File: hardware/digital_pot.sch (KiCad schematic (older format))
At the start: 100 parts, among them J8 Conn_02x08_Odd_Even, U10 MCP42010, U11 ADA4898-3, U12 ADA4898-3, U13 MCP42010, U14 MCP42010, U15 MCP42050, U16 MCP42050, U17 MCP42050, U2 ADA4898-3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

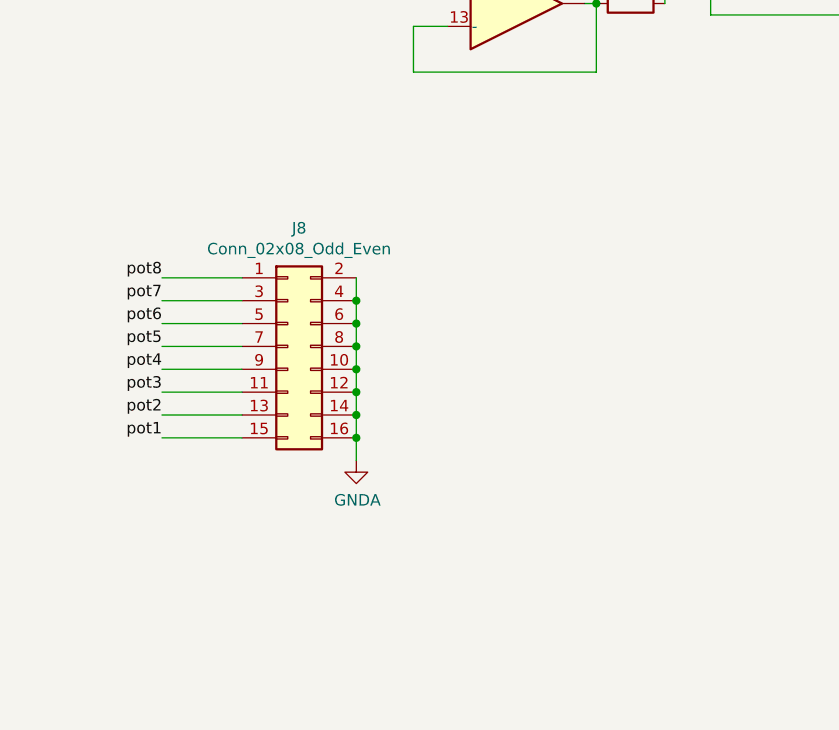
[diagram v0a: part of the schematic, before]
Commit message: layout gotów, do wyeliminowania błedy DRC
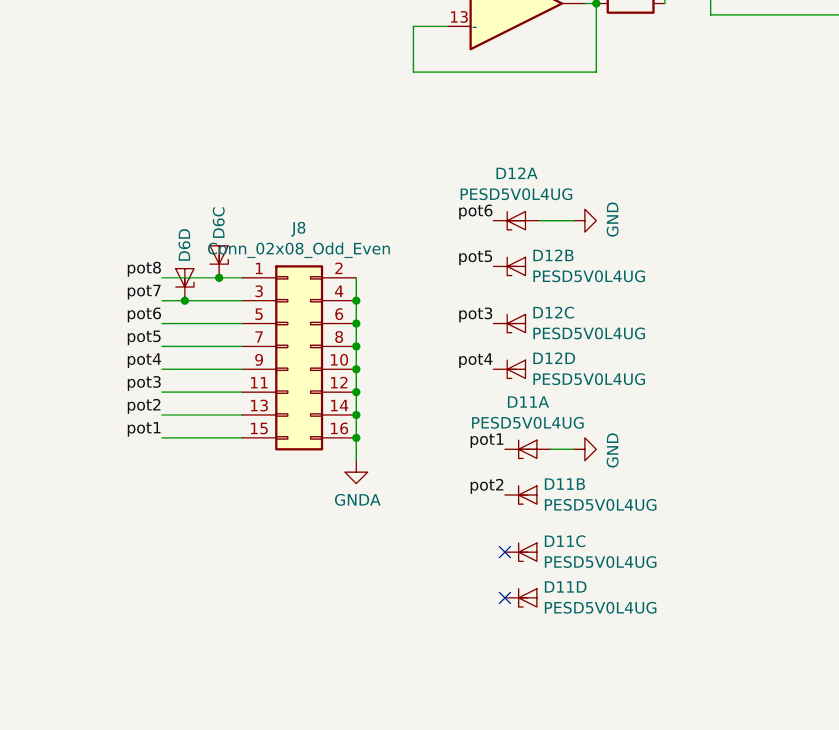
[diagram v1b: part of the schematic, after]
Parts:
- added D11, D12, D6: PESD5V0L4UG, Package_TO_SOT_SMD:SOT-353_SC-70-5, symbol Power_Protection:PESD5V0L4UG
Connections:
- net GND: now also D11.2 (A), D12.2 (A)
- net pot1: now also D11.1 (K1)
- net pot2: now also D11.3 (K2)
- net pot3: now also D12.4 (K3)
- net pot4: now also D12.5 (K4)
- net pot5: now also D12.3 (K2)
- net pot6: now also D12.1 (K1)
- net pot7: now also D6.5 (K4)
- net pot8: now also D6.4 (K3)
- no-connect marks 1 -> 3
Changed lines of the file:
@@
 	9500 9300 9850 9300
 Wire Wire Line
-	9850 9200 9500 9200
-Wire Wire Line
-	9500 9100 9850 9100
+	9850 9200 9600 9200
+Wire Wire Line
+	9500 9100 9750 9100
 Text Label 9500 9100 2    50   ~ 0
 pot8
@@
 Wire Wire Line
 	10350 9700 10350 9800
+$Comp
+L Power_Protection:PESD5V0L4UG D?
+U 3 1 5DD9CDD5
+P 9750 9000
+AR Path="/5CDEAB6D/5DD9CDD5" Ref="D?"  Part="3"
+AR Path="/5CDEABB2/5DD9CDD5" Ref="D6"  Part="3"
+F 0 "D6" H 9818 9000 50  0000 L CNN
+F 1 "PESD5V0L4UG" H 9818 8955 50  0001 L CNN
+F 2 "Package_TO_SOT_SMD:SOT-353_SC-70-5" H 9750 9000 50  0001 C CNN
+F 3 "https://assets.nexperia.com/documents/data-sheet/PESDXL4UF_G_W.pdf" H 9750 9000 50  0001 C CNN
+	3    9750 9000
+	0    -1   -1   0
+$EndComp
+$Comp
+L Power_Protection:PESD5V0L4UG D?
+U 4 1 5DD9CDDB
+P 9600 9100
+AR Path="/5CDEAB6D/5DD9CDDB" Ref="D?"  Part="4"
+AR Path="/5CDEABB2/5DD9CDDB" Ref="D6"  Part="4"
+F 0 "D6" H 9668 9100 50  0000 L CNN
+F 1 "PESD5V0L4UG" H 9668 9055 50  0001 L CNN
+F 2 "Package_TO_SOT_SMD:SOT-353_SC-70-5" H 9600 9100 50  0001 C CNN
+F 3 "https://assets.nexperia.com/documents/data-sheet/PESDXL4UF_G_W.pdf" H 9600 9100 50  0001 C CNN
+	4    9600 9100
+	0    -1   -1   0
+$EndComp
+Connection ~ 9750 9100
+Wire Wire Line
+	9750 9100 9850 9100
+Connection ~ 9600 9200
+Wire Wire Line
+	9600 9200 9500 9200
+$Comp
+L Power_Protection:PESD5V0L4UG D12
+U 1 1 5DE7618B
+P 11050 8850
+F 0 "D12" H 11050 9055 50  0000 C CNN
+F 1 "PESD5V0L4UG" H 11050 8964 50  0000 C CNN
+F 2 "Package_TO_SOT_SMD:SOT-353_SC-70-5" H 11050 8850 50  0001 C CNN
+F 3 "https://assets.nexperia.com/documents/data-sheet/PESDXL4UF_G_W.pdf" H 11050 8850 50  0001 C CNN
+	1    11050 8850
+	1    0    0    -1
+$EndComp
+$Comp
+L Power_Protection:PESD5V0L4UG D12
+U 2 1 5DE77CC7
+P 11050 9050
+F 0 "D12" H 11118 9096 50  0000 L CNN
+F 1 "PESD5V0L4UG" H 11118 9005 50  0000 L CNN
+F 2 "Package_TO_SOT_SMD:SOT-353_SC-70-5" H 11050 9050 50  0001 C CNN
+F 3 "https://assets.nexperia.com/documents/data-sheet/PESDXL4UF_G_W.pdf" H 11050 9050 50  0001 C CNN
+	2    11050 9050
+	1    0    0    -1
+$EndComp
+$Comp
+L Power_Protection:PESD5V0L4UG D12
+U 3 1 5DE7A9F7
+P 11050 9300
+F 0 "D12" H 11118 9346 50  0000 L CNN
+F 1 "PESD5V0L4UG" H 11118 9255 50  0000 L CNN
+F 2 "Package_TO_SOT_SMD:SOT-353_SC-70-5" H 11050 9300 50  0001 C CNN
+F 3 "https://assets.nexperia.com/documents/data-sheet/PESDXL4UF_G_W.pdf" H 11050 9300 50  0001 C CNN
+	3    11050 9300
+	1    0    0    -1
+$EndComp
+$Comp
+L Power_Protection:PESD5V0L4UG D12
+U 4 1 5DE7C364
+P 11050 9500
+F 0 "D12" H 11118 9546 50  0000 L CNN
+F 1 "PESD5V0L4UG" H 11118 9455 50  0000 L CNN
+F 2 "Package_TO_SOT_SMD:SOT-353_SC-70-5" H 11050 9500 50  0001 C CNN
+F 3 "https://assets.nexperia.com/documents/data-sheet/PESDXL4UF_G_W.pdf" H 11050 9500 50  0001 C CNN
+	4    11050 9500
+	1    0    0    -1
+$EndComp
+$Comp
+L Power_Protection:PESD5V0L4UG D11
+U 1 1 5DE7E45C
+P 11100 9850
+F 0 "D11" H 11100 10055 50  0000 C CNN
+F 1 "PESD5V0L4UG" H 11100 9964 50  0000 C CNN
+F 2 "Package_TO_SOT_SMD:SOT-353_SC-70-5" H 11100 9850 50  0001 C CNN
+F 3 "https://assets.nexperia.com/documents/data-sheet/PESDXL4UF_G_W.pdf" H 11100 9850 50  0001 C CNN
+	1    11100 9850
+	1    0    0    -1
+$EndComp
+$Comp
+L Power_Protection:PESD5V0L4UG D11
+U 2 1 5DE7E462
+P 11100 10050
+F 0 "D11" H 11168 10096 50  0000 L CNN
+F 1 "PESD5V0L4UG" H 11168 10005 50  0000 L CNN
+F 2 "Package_TO_SOT_SMD:SOT-353_SC-70-5" H 11100 10050 50  0001 C CNN
+F 3 "https://assets.nexperia.com/documents/data-sheet/PESDXL4UF_G_W.pdf" H 11100 10050 50  0001 C CNN
+	2    11100 10050
+	1    0    0    -1
+$EndComp
+$Comp
+L Power_Protection:PESD5V0L4UG D11
+U 3 1 5DE7E468
+P 11100 10300
+F 0 "D11" H 11168 10346 50  0000 L CNN
+F 1 "PESD5V0L4UG" H 11168 10255 50  0000 L CNN
+F 2 "Package_TO_SOT_SMD:SOT-353_SC-70-5" H 11100 10300 50  0001 C CNN
+F 3 "https://assets.nexperia.com/documents/data-sheet/PESDXL4UF_G_W.pdf" H 11100 10300 50  0001 C CNN
+	3    11100 10300
+	1    0    0    -1
+$EndComp
+$Comp
+L Power_Protection:PESD5V0L4UG D11
+U 4 1 5DE7E46E
+P 11100 10500
+F 0 "D11" H 11168 10546 50  0000 L CNN
+F 1 "PESD5V0L4UG" H 11168 10455 50  0000 L CNN
+F 2 "Package_TO_SOT_SMD:SOT-353_SC-70-5" H 11100 10500 50  0001 C CNN
+F 3 "https://assets.nexperia.com/documents/data-sheet/PESDXL4UF_G_W.pdf" H 11100 10500 50  0001 C CNN
+	4    11100 10500
+	1    0    0    -1
+$EndComp
+Text Label 10950 8850 2    50   ~ 0
+pot6
+Text Label 10950 9050 2    50   ~ 0
+pot5
+Text Label 10950 9500 2    50   ~ 0
+pot4
+Text Label 10950 9300 2    50   ~ 0
+pot3
+$Comp
+L power:GND #PWR0183
+U 1 1 5DEE9530
+P 11300 8850
+F 0 "#PWR0183" H 11300 8600 50  0001 C CNN
+F 1 "GND" H 11305 8677 50  0000 C CNN
+F 2 "" H 11300 8850 50  0001 C CNN
+F 3 "" H 11300 8850 50  0001 C CNN
+	1    11300 8850
+	0    -1   -1   0
+$EndComp
+Wire Wire Line
+	11300 8850 11150 8850
+$Comp
+L power:GND #PWR0184
+U 1 1 5DF1F5A6
+P 11300 9850
+F 0 "#PWR0184" H 11300 9600 50  0001 C CNN
+F 1 "GND" H 11305 9677 50  0000 C CNN
+F 2 "" H 11300 9850 50  0001 C CNN
+F 3 "" H 11300 9850 50  0001 C CNN
+	1    11300 9850
+	0    -1   1    0
+$EndComp
+Wire Wire Line
+	11200 9850 11300 9850
+Text Label 11000 10050 2    50   ~ 0
+pot2
+Text Label 11000 9850 2    50   ~ 0
+pot1
+NoConn ~ 11000 10300
+NoConn ~ 11000 10500
 $EndSCHEMATC
